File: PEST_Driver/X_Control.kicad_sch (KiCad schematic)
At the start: 68 parts, among them J1 Conn_01x02, J2 Conn_01x02, J3 Conn_01x02, J4 Conn_01x02, J5 Conn_01x02, J6 Conn_01x02, J7 Conn_01x02, J8 Conn_01x02, U19 74HC4051, U2 74HC4051, U20 74HC4051, U21 74HC595, U22 74HC4051, U3 74HC4051

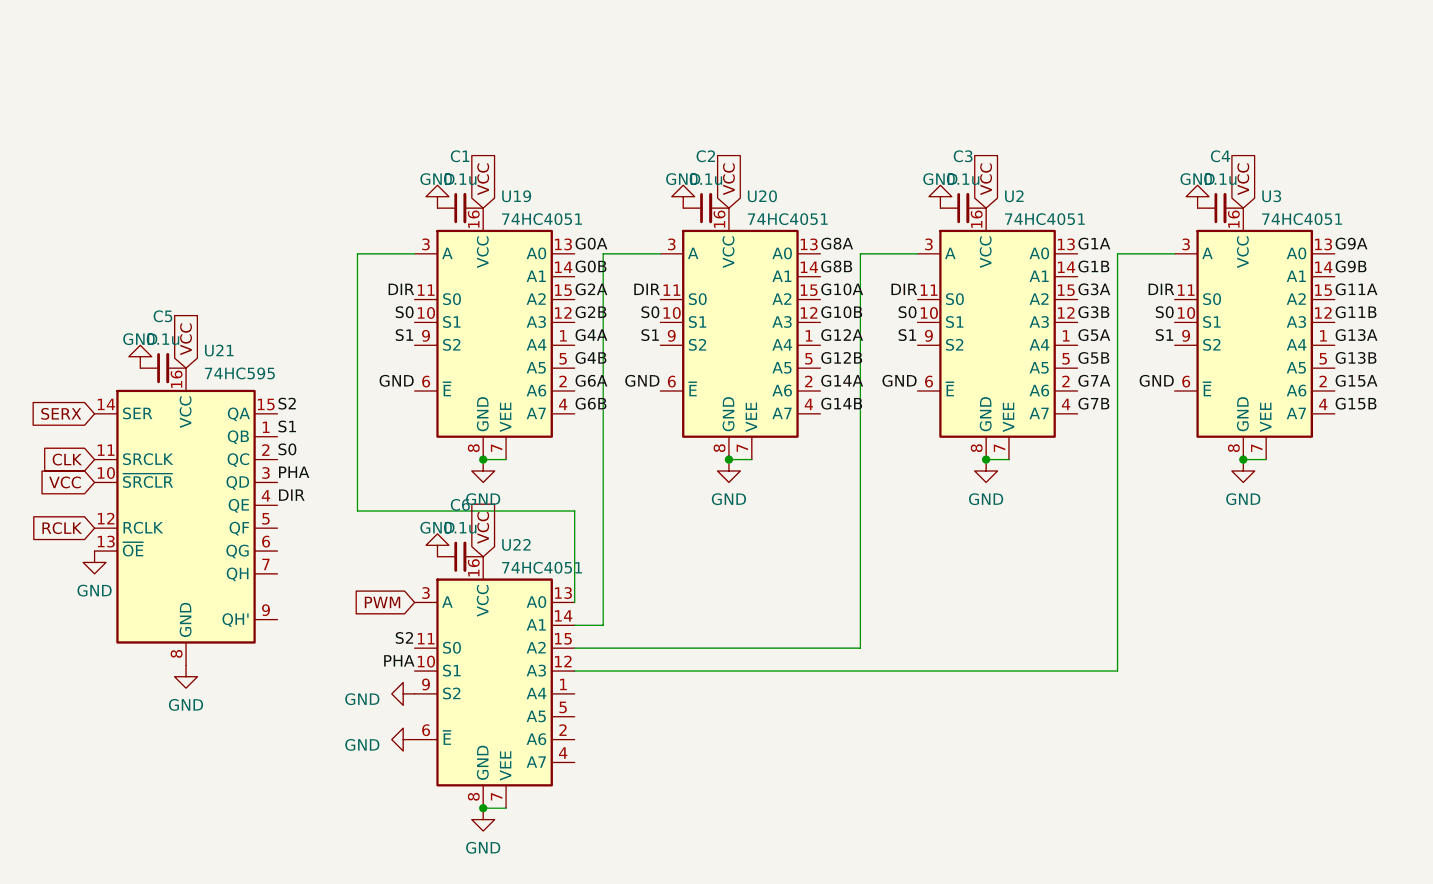
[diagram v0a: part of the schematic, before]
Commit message: Added independent signal ground to schematic
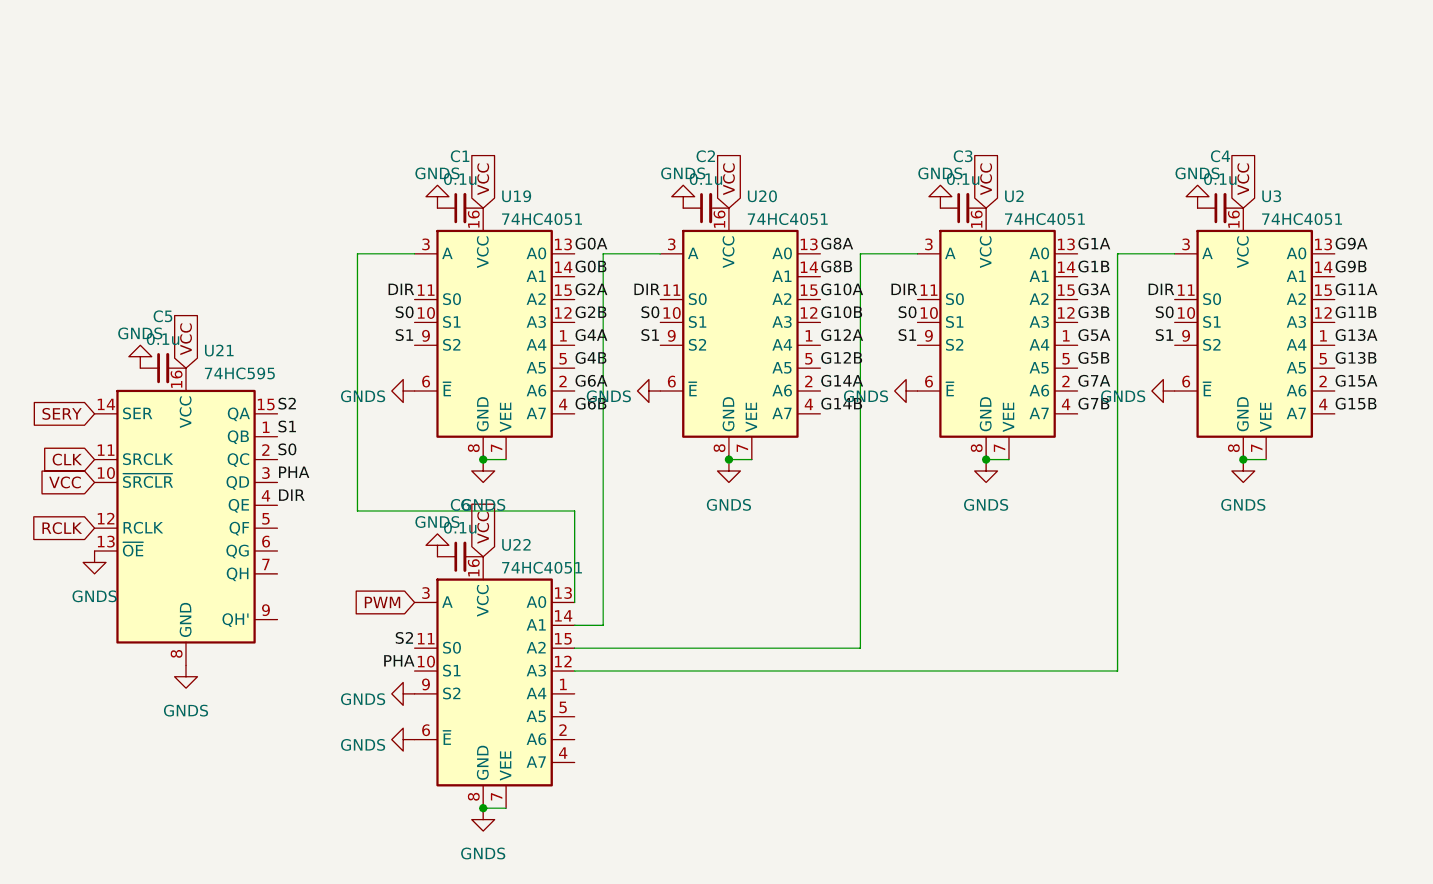
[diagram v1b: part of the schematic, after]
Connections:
- net GND: no longer C1.1, C2.1, C3.1, C4.1, C5.1, C6.1, U19.6 (~{E}), U19.7 (VEE), U19.8 (GND), U2.6 (~{E}), U2.7 (VEE), U2.8 (GND), U20.6 (~{E}), U20.7 (VEE), U20.8 (GND), U21.13 (~{OE}), U21.8 (GND), U22.6 (~{E}), U22.7 (VEE), U22.8 (GND), U22.9 (S2), U3.6 (~{E}), U3.7 (VEE), U3.8 (GND)
- net SERX renamed SERY
- new net GNDS: C1.1, C2.1, C3.1, C4.1, C5.1, C6.1, U19.6 (~{E}), U19.7 (VEE), U19.8 (GND), U2.6 (~{E}), U2.7 (VEE), U2.8 (GND), U20.6 (~{E}), U20.7 (VEE), U20.8 (GND), U21.13 (~{OE}), U21.8 (GND), U22.6 (~{E}), U22.7 (VEE), U22.8 (GND), U22.9 (S2), U3.6 (~{E}), U3.7 (VEE), U3.8 (GND)

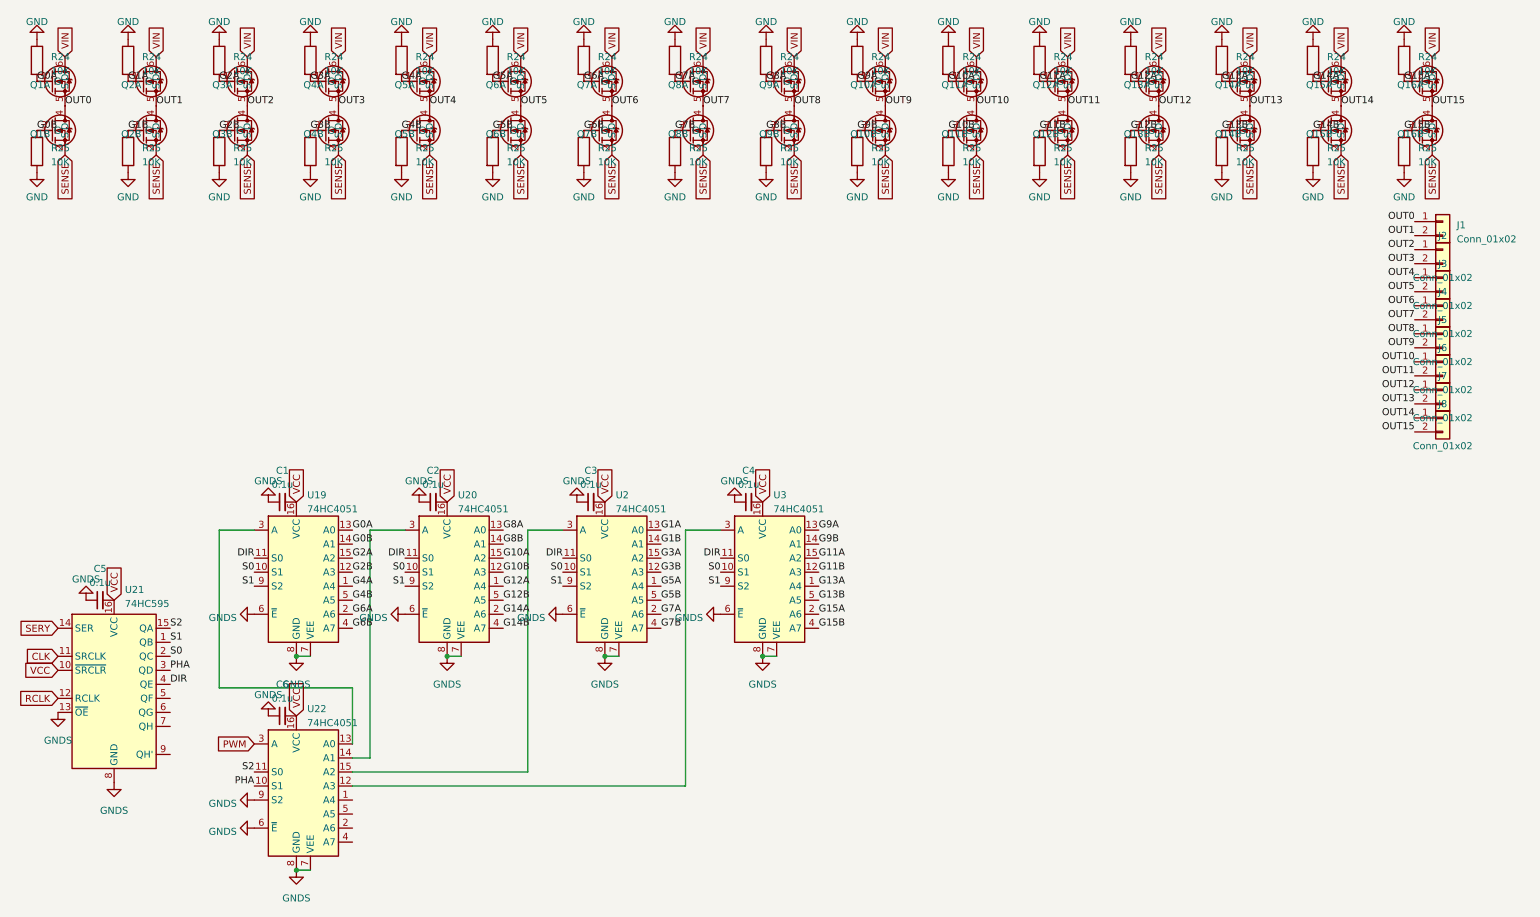
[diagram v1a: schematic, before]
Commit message: Finished wiring independent MOSFET and logic grounds
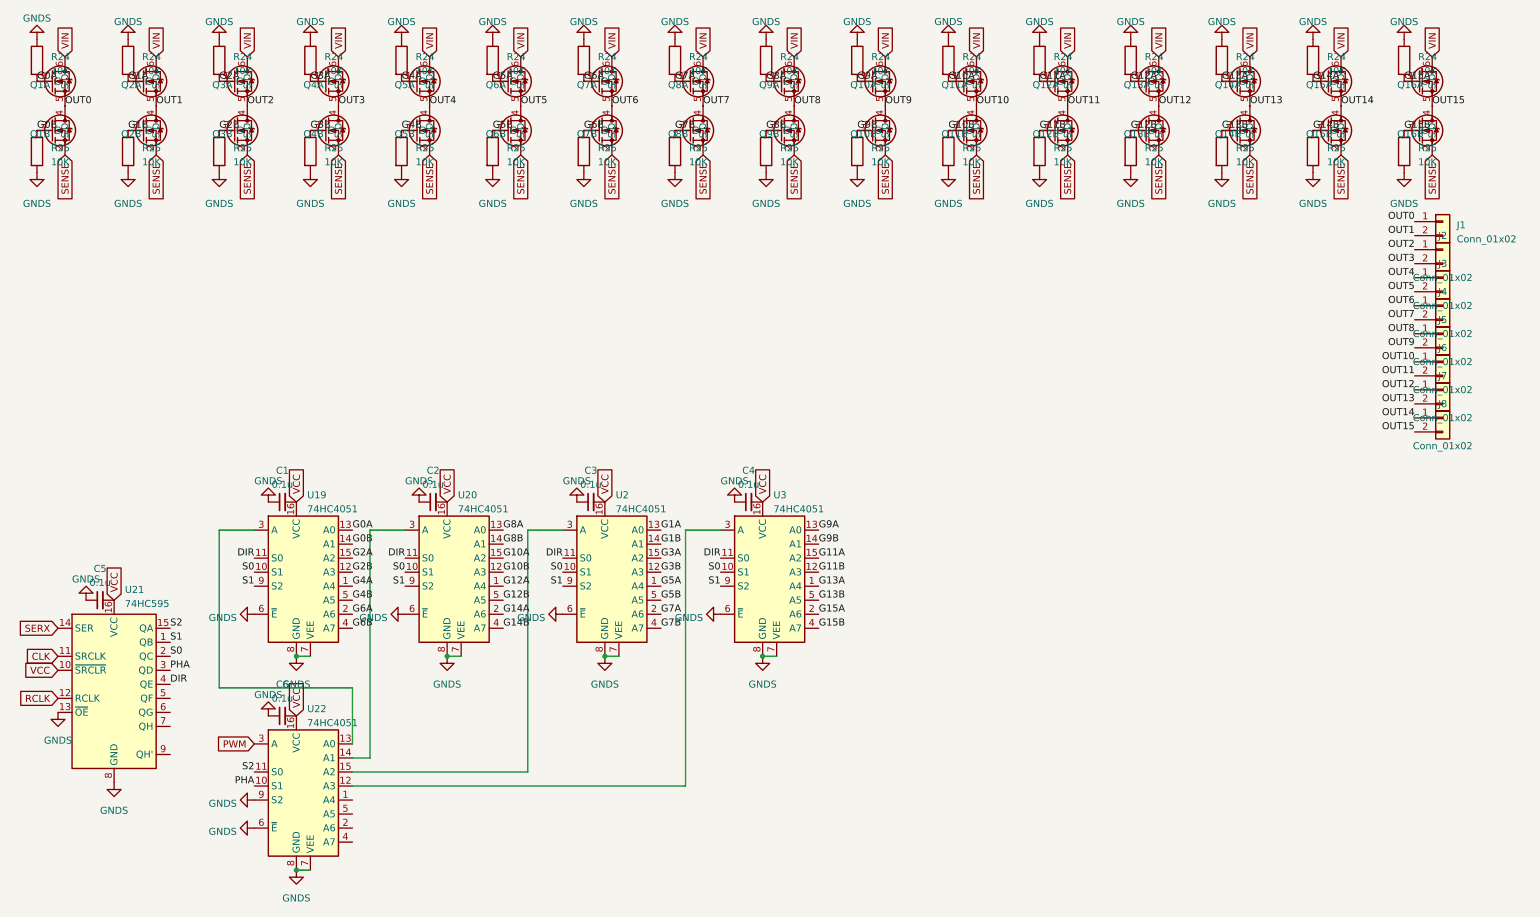
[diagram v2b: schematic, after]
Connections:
- net GND is gone; now on net GNDS: R24.1, R24.1, R24.1, R24.1, R24.1, R24.1, R24.1, R24.1, R24.1, R24.1, R24.1, R24.1, R24.1, R24.1, R24.1, R24.1, R25.2, R25.2, R25.2, R25.2, R25.2, R25.2, R25.2, R25.2, R25.2, R25.2, R25.2, R25.2, R25.2, R25.2, R25.2, R25.2
- net SERY renamed SERX

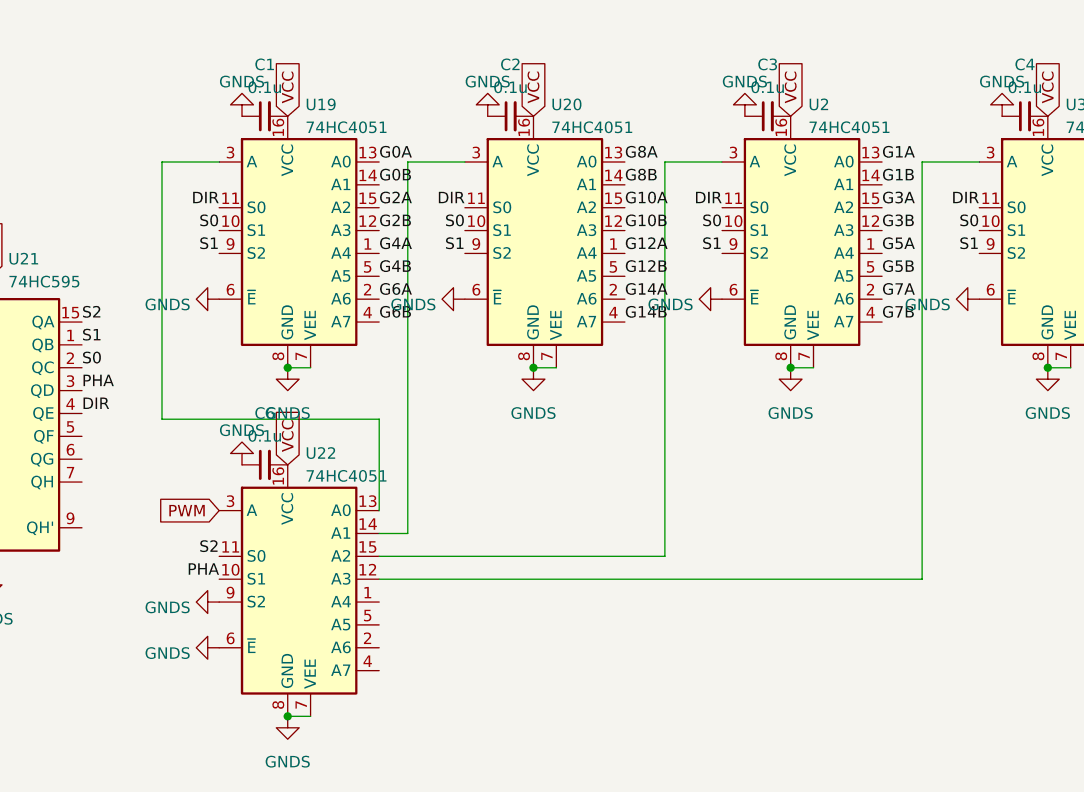
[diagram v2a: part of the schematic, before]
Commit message: Added more pulldown resistors to PEST Driver
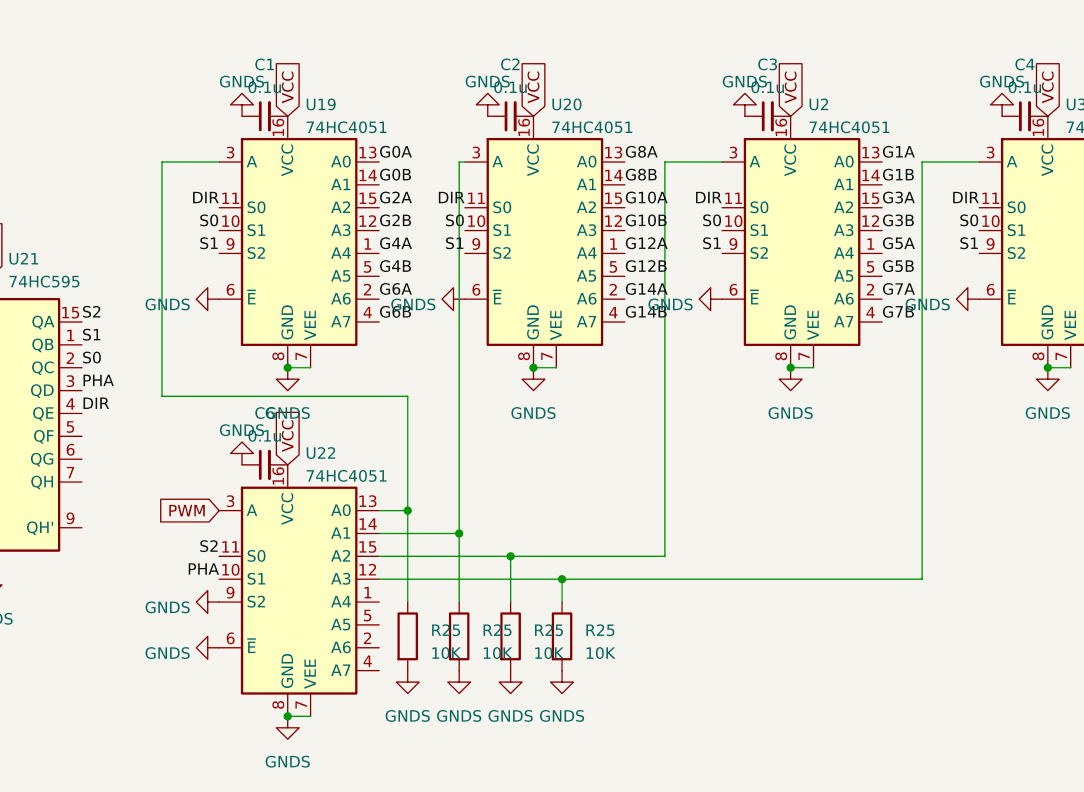
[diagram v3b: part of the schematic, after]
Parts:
- added R25 (x4): 10K, Resistor_SMD:R_0402_1005Metric, symbol Device:R
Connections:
- net GNDS: now also R25.2, R25.2, R25.2, R25.2
- net at U22.12 (A3), U3.3 (A): now also R25.1
- net at U19.3 (A), U22.13 (A0): now also R25.1
- net at U20.3 (A), U22.14 (A1): now also R25.1
- net at U2.3 (A), U22.15 (A2): now also R25.1
